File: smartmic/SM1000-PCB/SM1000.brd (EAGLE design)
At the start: 100 x 80 mm, 155 parts, among them CN1 HDR100-6, CN2 MOLEX-MINI-B-SMT, CN3 RASM712PX, CN4 RJ-45, CN5 MJ-3523-SMT, CN6 MJ-3523-SMT, CN7 MJ-3523-SMT, CN8 MJ-3523-SMT, CN9 MJ-3523-SMT, IC1 DIL-16, J1 JMP-2PIN, J2 JMP-2PIN, J3 JMP-2PIN, J5 JMPR-3PIN, Q1 MMBT4401, Q2 MMBT4401, SW1 SW-SPST-2-1437565-0, SW2 SW-SPST-2-1437565-0, SW3 DPDT, T1 SM-LP-5001, T2 SM-LP-5001, U1 STM32F407, U2 LD3985M33R, U3 STMPS2141, U4 EMIF02-USB03F2, U5 TPS54329E, U6 LMV341, U7 LMV341, U8 LM386M-1, X1 8.0MHz

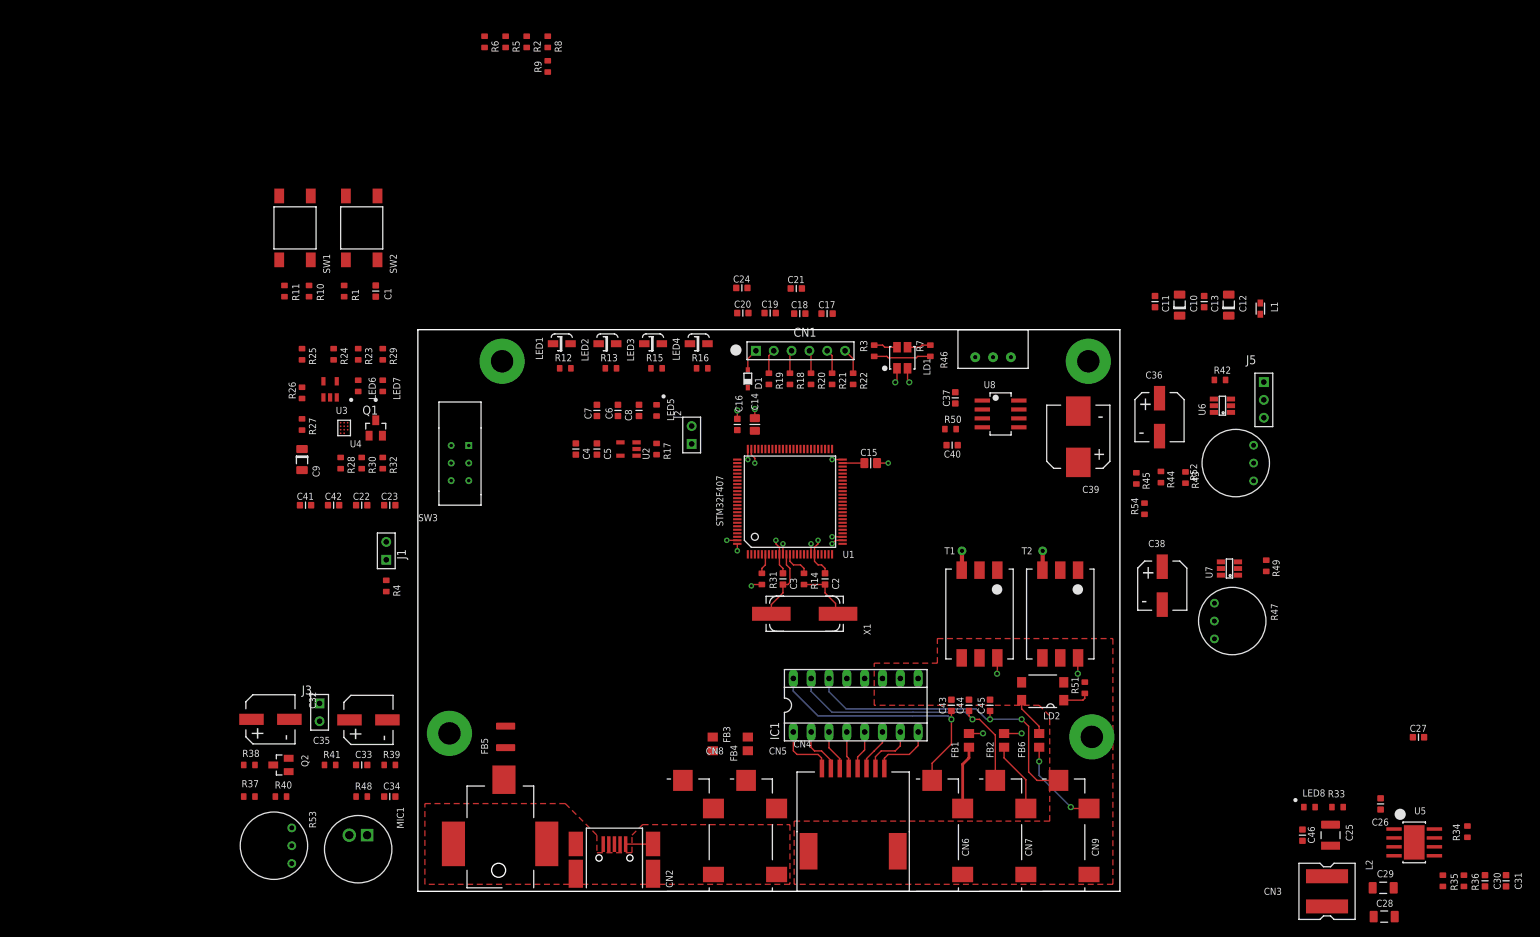
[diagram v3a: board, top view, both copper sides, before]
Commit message: 
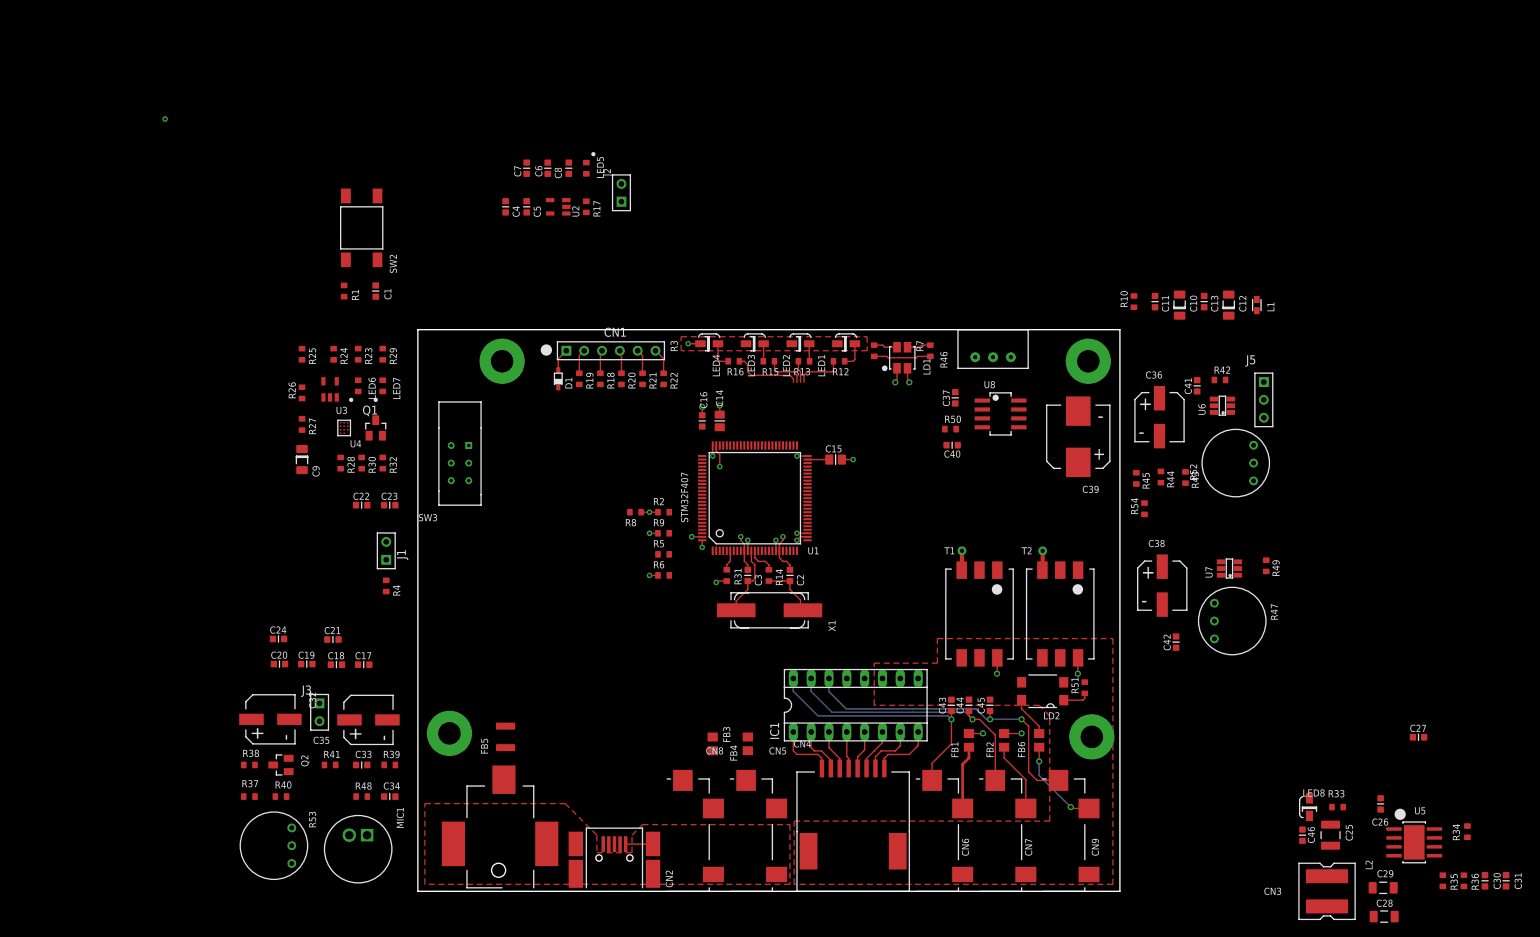
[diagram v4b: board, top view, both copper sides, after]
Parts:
- removed R11: 220K,1%, _Coherix:R0603
- removed SW1: SW-SPST-2-1437565-0, _RoweTel:SW-SPST-TE-2-1437565-0
- LED1, LED2: value LED-RED -> LED-RED,RA
- LED3: value LED-GRN -> LED-GRN,RA
- LED4: value LED-YEL -> LED-YEL,RA
- LED5: value LED-RED -> LED-RED,V
- LED6, LED7: value LED-GRN -> LED-GRN,V
- LED8: device _Coherix:CHIP-LED-0603 -> _RoweTel:LTST-S2200K
- R10: value 330,1% -> 47,1%
- moved C41 128.1 mm to (111.0, 72.0), turned to 90 degrees
- moved C42 121.6 mm to (108.0, 35.5), turned to 90 degrees
- moved R10 117.5 mm to (102.0, 84.0)
- moved C17 82.8 mm to (-7.71, 32.3)
- moved C18 82.8 mm to (-11.6, 32.3)
- moved C19 82.8 mm to (-15.8, 32.4)
- moved C20 82.8 mm to (-19.7, 32.4)
- moved C21 82.8 mm to (-12.1, 35.9)
- moved C24 82.8 mm to (-19.9, 36.0)
- moved R6 80.2 mm to (35.0, 45.0), turned to 0 degrees
- moved R5 76.4 mm to (35.0, 48.0), turned to 0 degrees
- moved R2 69.8 mm to (35.0, 54.0), turned to 0 degrees
- moved R9 68.5 mm to (35.0, 51.0), turned to 0 degrees
- moved R8 68.2 mm to (31.0, 54.0), turned to 0 degrees
- moved LED1 40.5 mm to (61.0, 78.0)
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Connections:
- removed net WAKE_UP: R10.1, U1.23
- net GND: no longer R11.1
- net N$4: now also C10.1, C11.1, U1.21; no longer R11.2, SW1.1, SW1.2
- net N$5: now also R10.1; no longer C10.1, C11.1, U1.21
- net STLINK: now also U1.23
- net VDD: no longer SW1.3, SW1.4
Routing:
- net LED-ERR: track 0.00 -> 9.82 mm
- net LED-PWR: track 0.00 -> 6.79 mm
- net LED-RT: track 0.00 -> 5.79 mm
- net GND: track 35.3 -> 40.5 mm, vias 11 -> 13
- net N$20: track 0.00 -> 3.80 mm
- net N$16: track 0.00 -> 3.80 mm
- net LED-PTT: track 0.00 -> 3.12 mm
- net N$18: track 0.00 -> 2.52 mm
- net N$17: track 0.00 -> 2.52 mm
- net VDD: track 12.2 -> 14.6 mm, vias 8 -> 10
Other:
- board text removed: "Pull-ups & Pull-downs"

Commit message: Add polarity protection. Add 47Ohm resistor to VREF+ circuit Continue PCB layout
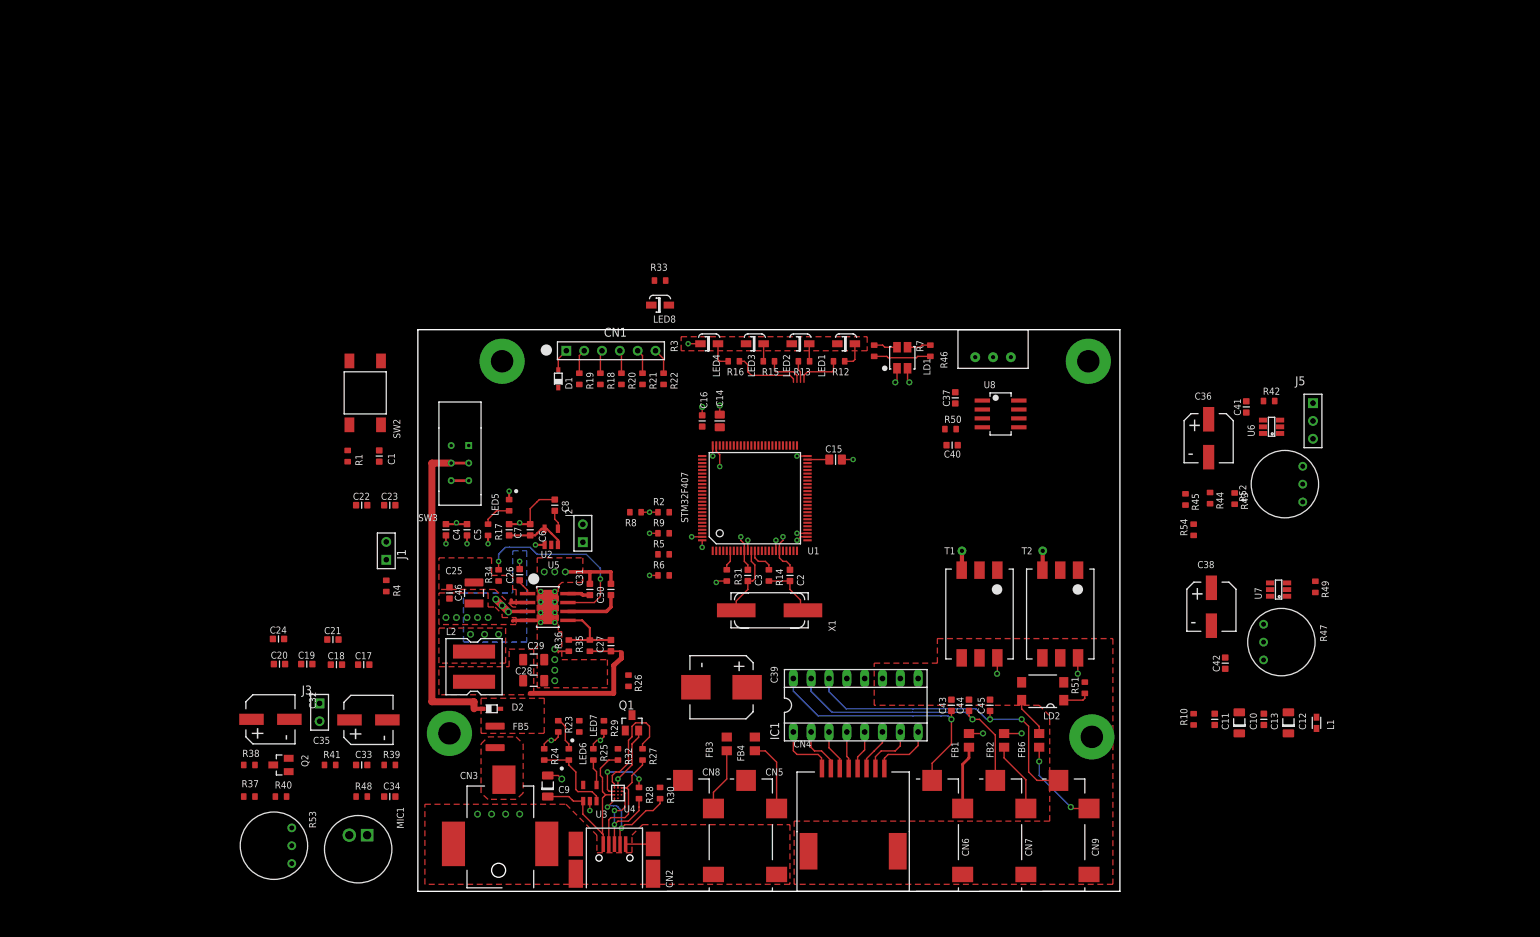
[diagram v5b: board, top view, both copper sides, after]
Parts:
- added D2: BAT60J, _RoweTel:SOD323R_INFINEON
- moved R34 142.7 mm to (11.5, 45.0), turned to 90 degrees
- moved C31 136.9 mm to (24.5, 43.0), turned to 90 degrees
- moved R36 131.8 mm to (21.5, 35.0)
- moved C30 131.2 mm to (27.5, 43.0), turned to 90 degrees
- moved U5 127.9 mm to (18.5, 40.5)
- moved C26 126.9 mm to (14.5, 45.1)
- moved C25 126.8 mm to (8.00, 42.5)
- moved C46 126.3 mm to (4.50, 42.5)
- moved R35 126.0 mm to (24.5, 35.0)
- moved C28 125.7 mm to (16.5, 30.0)
- moved L2 125.6 mm to (8.00, 32.0)
- moved C29 125.3 mm to (16.5, 33.0)
- moved R33 122.2 mm to (34.5, 87.0)
- moved LED8 116.9 mm to (34.5, 83.5), turned to 270 degrees
- moved C27 115.8 mm to (27.5, 35.0), turned to 90 degrees
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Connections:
- net N$24 renamed SW
- removed net N$78: FB5.2, SW3.5
- new net N$24: D2.A, FB5.2
- new net N$80: D2.C, SW3.2, SW3.5
- net +VIN: now also SW3.3
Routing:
- net N$80: track 0.00 -> 47.5 mm
- net GND: track 40.5 -> 82.9 mm, vias 13 -> 43
- net +5V: track 0.00 -> 31.8 mm
- net N$42: track 0.00 -> 27.3 mm, vias 0 -> 2
- net VBUS: track 0.00 -> 26.9 mm
- net OTG_DM: track 0.00 -> 16.9 mm
- net N$23: track 0.00 -> 16.8 mm
- net N$28: track 0.00 -> 16.5 mm, vias 0 -> 2
- net N$22: track 0.00 -> 15.1 mm, vias 0 -> 2
- net OTG_OVR_CUR: track 0.00 -> 12.2 mm
- net +3.3V: track 0.00 -> 12.0 mm, vias 0 -> 6
- net N$30: track 0.00 -> 11.3 mm
- net N$76: track 0.00 -> 10.4 mm
- net OTG_DP: track 0.00 -> 9.72 mm, vias 0 -> 2
- net N$75: track 0.00 -> 9.01 mm
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- added copper zone on layer 2, net +3.3V
- added copper zone on layer 1, net +5V
- added copper zone on layer 1, net +VIN
- added copper zone on layer 1, net N$24
- added copper zone on layer 1, net N$77
- added copper zone on layer 1, net SW
- added copper zone on layer 16, net SW
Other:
- board text removed: "5V -> 3.3V PWR"

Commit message: Change large electrolytic caps to ceramic for space reasons.
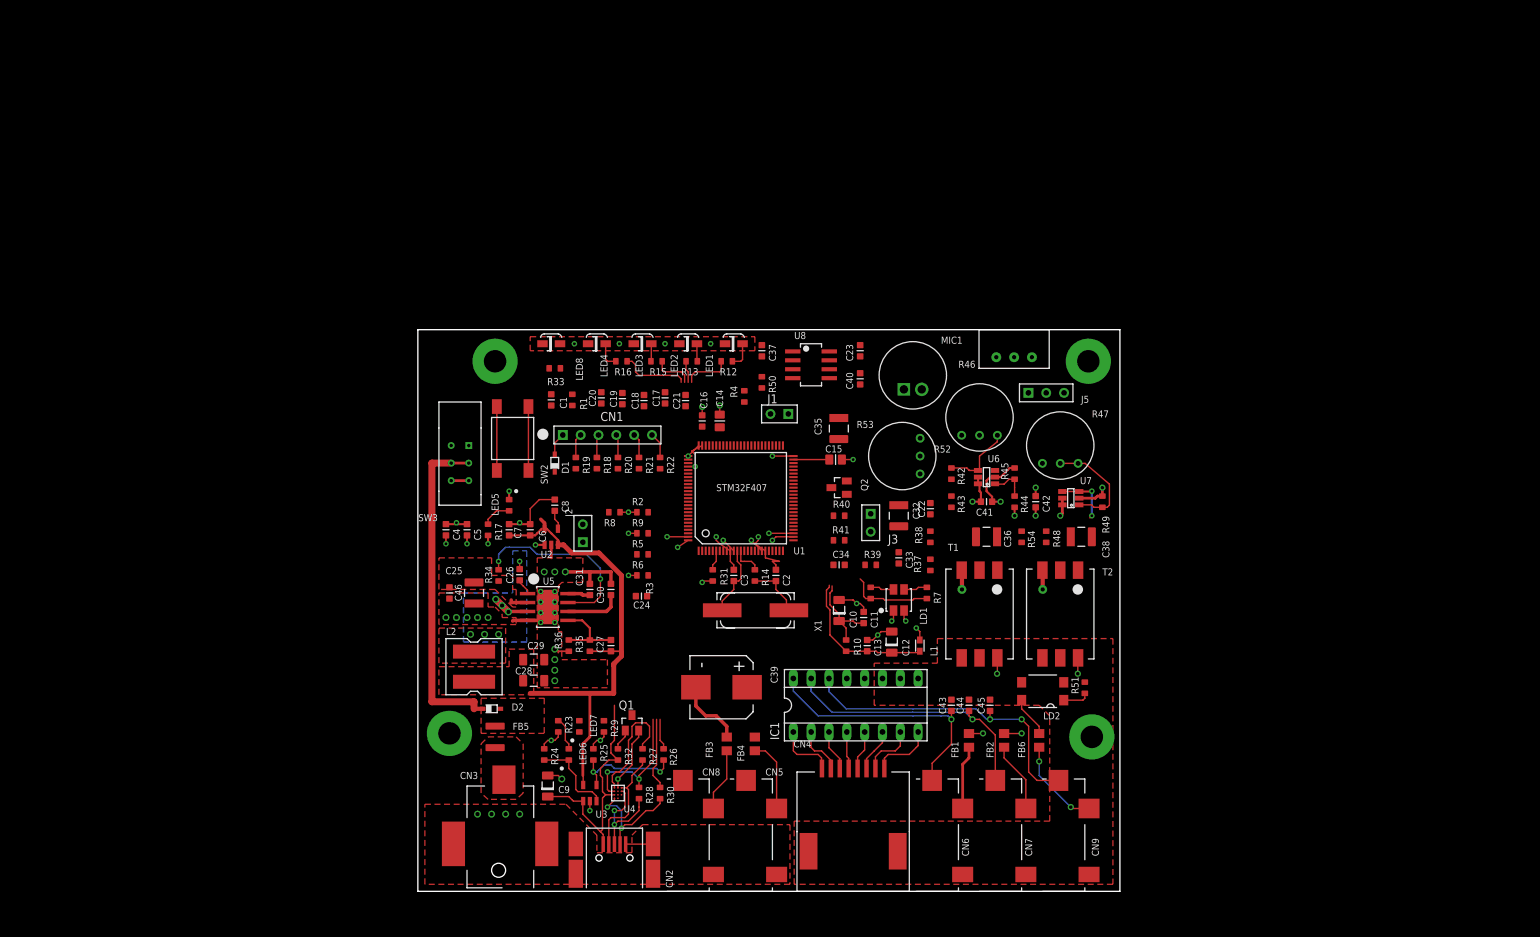
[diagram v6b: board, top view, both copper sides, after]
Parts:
- C32, C35, C36, C38: value 100uF,16V -> 100uF,10V; device _RoweTel:CAP-CHEMI-F55 -> SM1000:C1210
- CN2: device _RoweTel:MOLEX-MINI-B-SMT -> SM1000:MOLEX-MINI-B-SMT
- LD1: device _RoweTel:LED-R/G -> SM1000:LED-R/G
- U1: device _RoweTel:LQFP100-14 -> SM1000:LQFP100-14
- moved R53 105.3 mm to (69.0, 62.0)
- moved R48 104.3 mm to (89.5, 50.5), turned to 270 degrees
- moved MIC1 103.9 mm to (70.5, 73.5), turned to 90 degrees
- moved R37 102.5 mm to (73.0, 46.5), turned to 270 degrees
- moved R38 102.3 mm to (73.0, 50.5), turned to 90 degrees
- moved C32 94.1 mm to (68.5, 53.5)
- moved R40 89.0 mm to (60.0, 53.5)
- moved Q2 88.8 mm to (60.0, 57.5)
- moved J3 83.0 mm to (64.5, 52.5)
- moved SH3 82.7 mm to (64.5, 52.5)
- moved C33 82.0 mm to (68.5, 47.5), turned to 90 degrees
- moved C22 81.0 mm to (73.0, 54.5), turned to 90 degrees
- moved R41 79.2 mm to (60.0, 50.0)
- moved C35 78.8 mm to (60.0, 65.9)
- moved R39 74.2 mm to (64.5, 46.5)
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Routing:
- net GND: track 82.9 -> 122.7 mm, vias 43 -> 51
- net +5V: track 31.8 -> 68.0 mm
- net N$5: track 0.00 -> 21.4 mm
- net VDD: track 14.6 -> 32.1 mm, vias 10 -> 15
- net N$90: track 0.00 -> 15.7 mm
- net N$4: track 0.00 -> 12.4 mm
- net N$31: track 3.74 -> 16.0 mm, vias 0 -> 2
- net OTG_ID: track 0.00 -> 10.3 mm
- net N$48: track 0.00 -> 10.3 mm
- net N$44: track 0.00 -> 9.80 mm
- net OTG_DP: track 9.72 -> 19.0 mm
- net NRST: track 0.00 -> 9.10 mm
- net VBUS: track 26.9 -> 35.0 mm
- net N$71: track 0.00 -> 8.09 mm, vias 0 -> 2
- net N$59: track 0.00 -> 5.51 mm
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
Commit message: Try commit again.
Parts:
- C23: value 100nF,16V -> 100nF,25V
- moved C18 30.8 mm to (56.5, 51.0), turned to 270 degrees
- moved C21 29.2 mm to (52.5, 44.5), turned to 180 degrees
- moved R6 26.9 mm to (56.5, 56.0), turned to 270 degrees
- moved C17 21.9 mm to (56.0, 63.5)
- moved C19 20.9 mm to (32.0, 49.5), turned to 180 degrees
- moved C24 5.94 mm to (37.0, 45.0), turned to 270 degrees
- moved R5 4.50 mm to (32.0, 52.5)
- moved R9 4.27 mm to (28.0, 52.5)
- moved J2 3.04 mm to (23.0, 54.0), turned to 0 degrees
- moved C35 2.61 mm to (60.6, 68.5), turned to 180 degrees
- moved X1 2.55 mm to (45.6, 39.5)
- moved C15 2.06 mm to (59.0, 63.5), turned to 90 degrees
- moved C2 2.00 mm to (49.0, 45.0)
- moved C3 2.00 mm to (43.0, 45.0)
- moved R14 2.00 mm to (46.0, 45.0)
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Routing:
- net +VIN: track 5.19 -> 101.2 mm, vias 0 -> 3
- net N$60: track 0.00 -> 93.4 mm, vias 0 -> 4
- net +5V: track 68.0 -> 146.9 mm, vias 0 -> 5
- net !CPPT!: track 0.00 -> 77.7 mm, vias 0 -> 4
- net N$36: track 0.00 -> 62.0 mm, vias 0 -> 2
- net NRST: track 9.10 -> 67.7 mm, vias 0 -> 2
- net OTG_OVR_CUR: track 12.2 -> 66.9 mm, vias 0 -> 4
- net VBUS: track 35.0 -> 85.4 mm, vias 0 -> 2
- net AIN2: track 0.00 -> 49.3 mm, vias 0 -> 2
- net GND: track 122.7 -> 169.8 mm, vias 51 -> 61
- net OTG_DM: track 16.9 -> 63.7 mm, vias 0 -> 2
- net AIN1: track 0.00 -> 46.7 mm, vias 0 -> 2
- net OTG_DP: track 19.0 -> 64.9 mm, vias 2 -> 4
- net OTG_ID: track 10.3 -> 55.1 mm, vias 0 -> 2
- net +3.3V: track 12.0 -> 56.1 mm
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- added copper zone on layer 16, net GND
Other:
- board text removed: "!RESET!"
- board text removed: "!TEST!"
- board text removed: "CPU ByPass Caps"
- board text removed: "MIC INTF."
- board text removed: "SPEAKER INTF."
- board text removed: "VREF & VDDA Bypass Caps"
- board text removed: "WAKE-UP"
